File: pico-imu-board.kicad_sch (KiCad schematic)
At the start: 5 parts, among them U1 RP2040, U2 MPU-9250

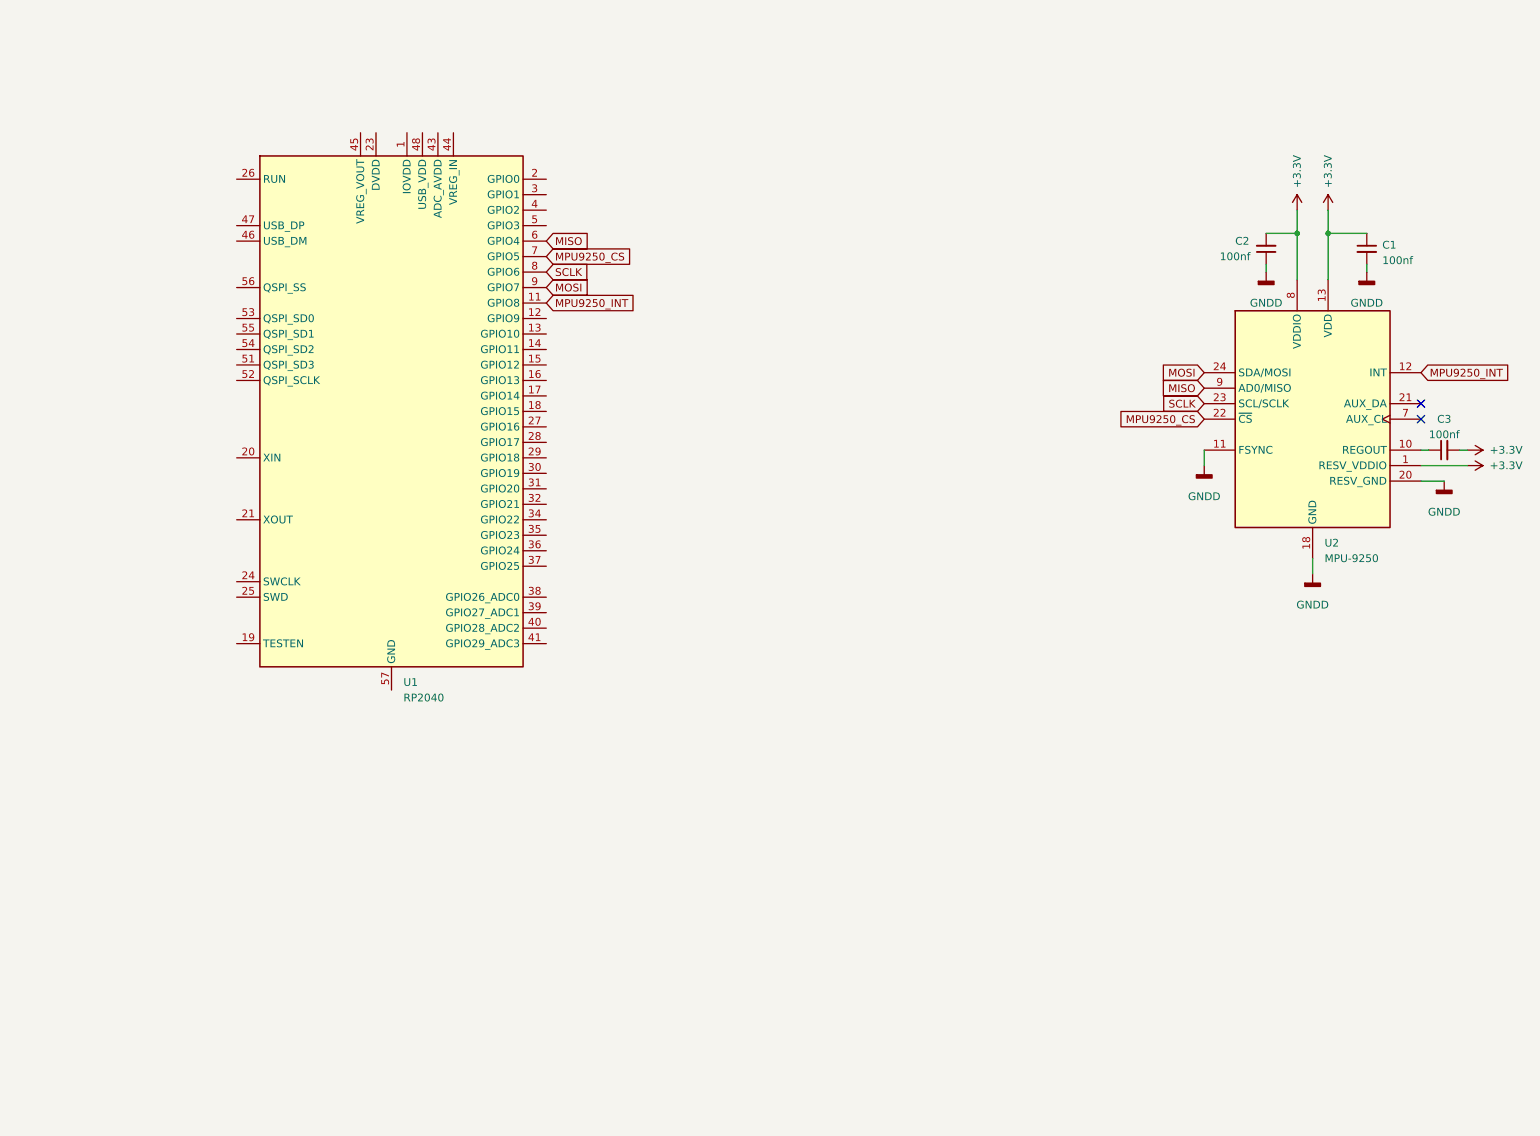
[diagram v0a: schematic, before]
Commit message: Added input supply to the schematic
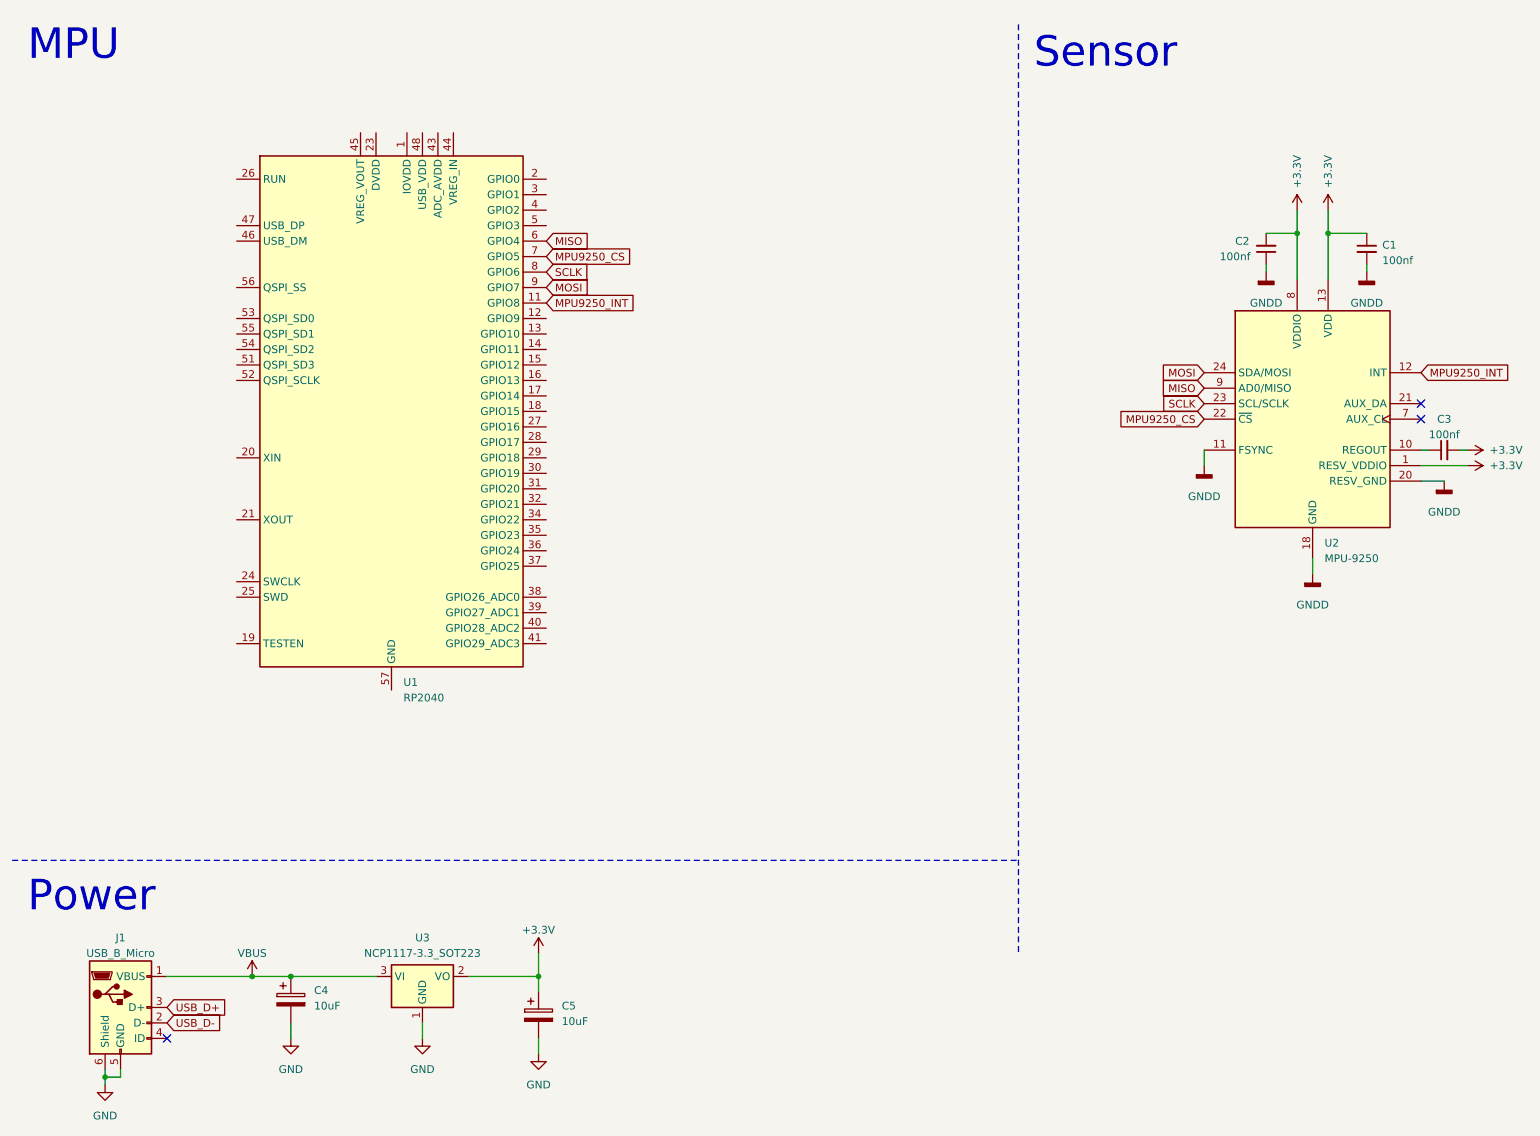
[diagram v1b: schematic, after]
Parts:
- added C4, C5: 10uF, symbol Device:C_Polarized
- added J1: USB_B_Micro, symbol Connector:USB_B_Micro
- added U3: NCP1117-3.3_SOT223, Package_TO_SOT_SMD:SOT-223-3_TabPin2, symbol Regulator_Linear:NCP1117-3.3_SOT223
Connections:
- net +3.3V: now also C5.1, U3.2 (VO)
- new net GND: C4.2, C5.2, J1.5 (GND), J1.6 (Shield), U3.1 (GND)
- new net USB_D+: J1.3 (D+)
- new net USB_D-: J1.2 (D-)
- new net VBUS: C4.1, J1.1 (VBUS), U3.3 (VI)
- no-connect marks 2 -> 3
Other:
- note added: "MPU"
- note added: "Power"
- note added: "Sensor"
